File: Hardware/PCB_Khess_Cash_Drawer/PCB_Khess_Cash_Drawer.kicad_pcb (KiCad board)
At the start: 2 copper layers, 92 x 84 mm, 17 parts, among them J1 Screw_Terminal_01x02, J2 Conn_01x02, J3 RJ11_Connector, J4 USB3_A, Q1 BUK9637-100E,118, U1 R-78B5.0-2.0

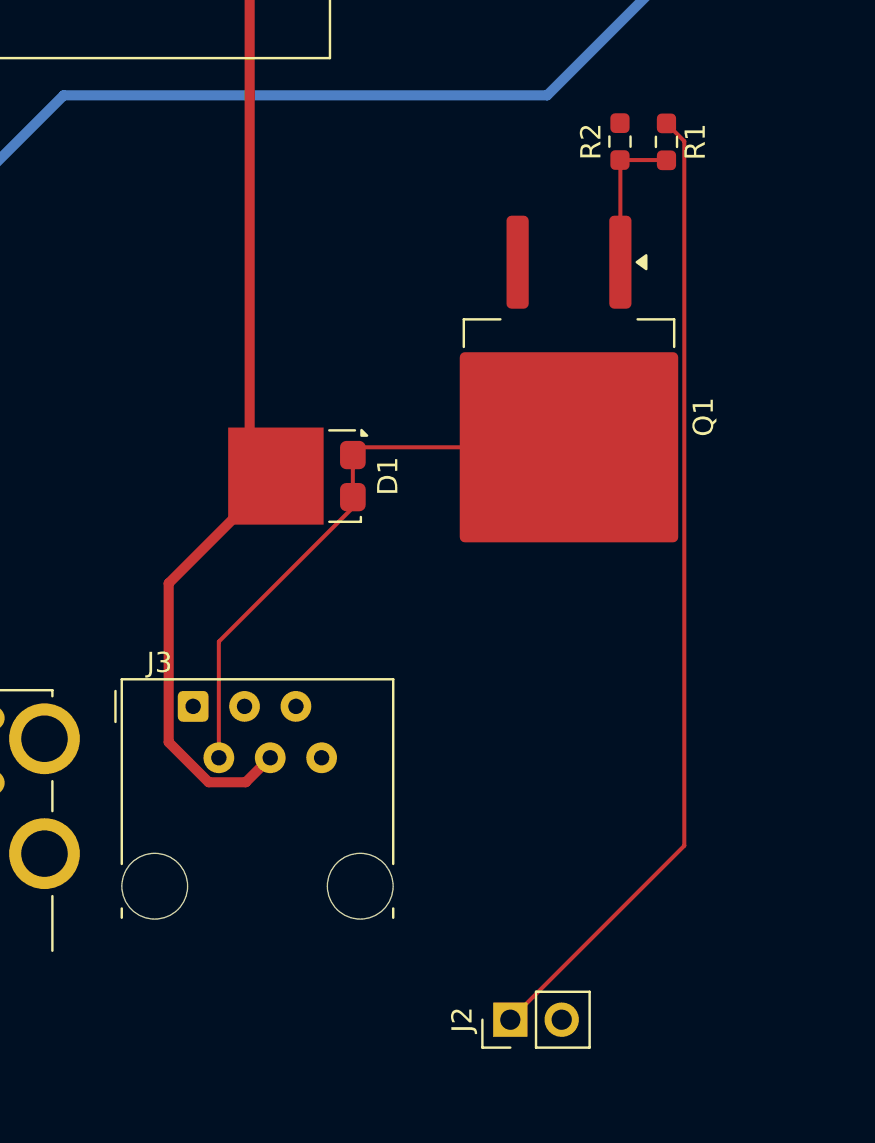
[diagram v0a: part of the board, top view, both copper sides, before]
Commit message: fix: fix pcb cash drawer
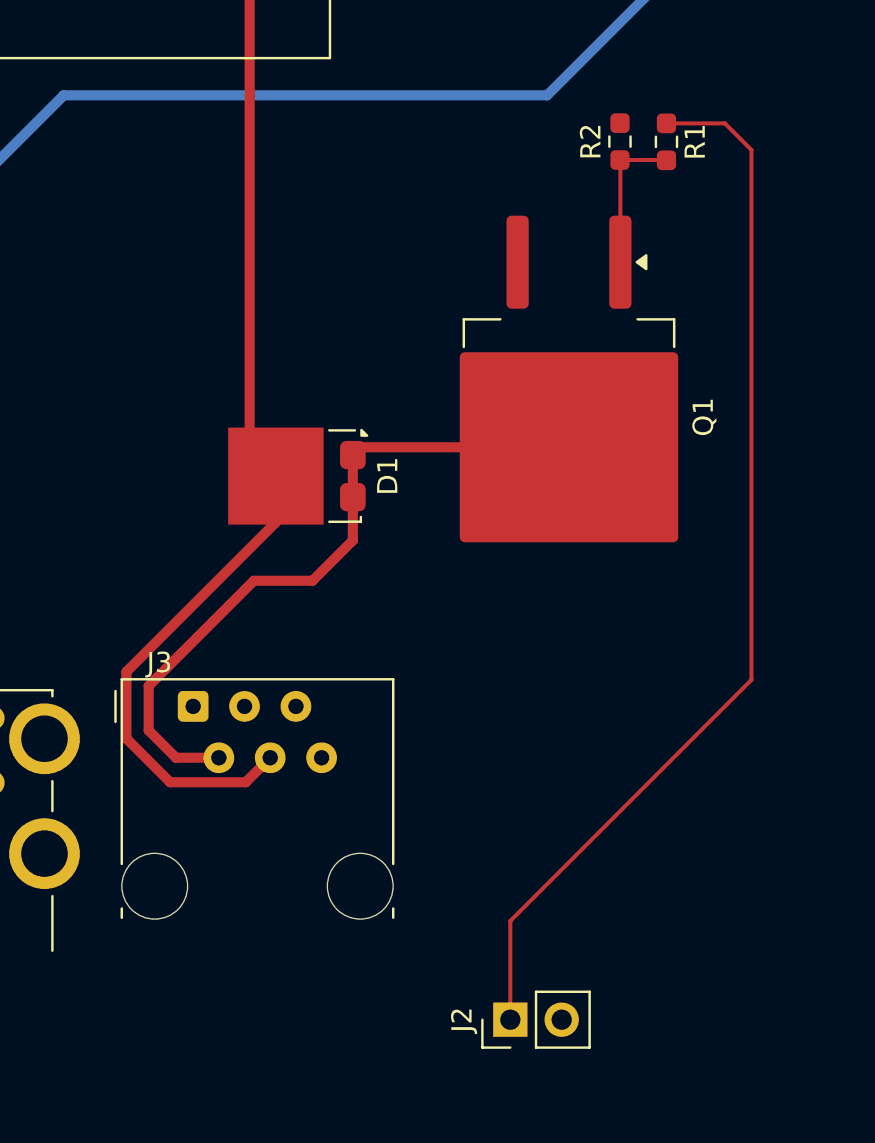
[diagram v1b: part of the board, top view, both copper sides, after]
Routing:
- net CASH_DRAWER_DRIVE: track 28.6 -> 34.9 mm
- net GPIO_CONTROL: track 48.2 -> 52.7 mm
- net CASH_DRAWER_VCC: track 63.1 -> 65.9 mm
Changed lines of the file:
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@@
 		(property ki_fp_filters "MountingHole*Pad*")
 		(sheetname "/")
-		(sheetfile "PCB_Khess.kicad_sch")
+		(sheetfile "PCB_Khess_Cash_Drawer.kicad_sch")
 		(attr exclude_from_pos_files)
 		(fp_circle
@@
 		(property ki_fp_filters "R_*")
 		(sheetname "/")
-		(sheetfile "PCB_Khess.kicad_sch")
+		(sheetfile "PCB_Khess_Cash_Drawer.kicad_sch")
 		(attr smd)
 		(fp_line
@@
 		(property ki_fp_filters "MountingHole*Pad*")
 		(sheetname "/")
-		(sheetfile "PCB_Khess.kicad_sch")
+		(sheetfile "PCB_Khess_Cash_Drawer.kicad_sch")
 		(attr exclude_from_pos_files)
 		(fp_circle
@@
 		(property ki_fp_filters "MountingHole*Pad*")
 		(sheetname "/")
-		(sheetfile "PCB_Khess.kicad_sch")
+		(sheetfile "PCB_Khess_Cash_Drawer.kicad_sch")
 		(attr exclude_from_pos_files)
 		(fp_circle
@@
 		(property ki_fp_filters "Converter*DCDC*RECOM*R*78B*2.0*")
 		(sheetname "/")
-		(sheetfile "PCB_Khess.kicad_sch")
+		(sheetfile "PCB_Khess_Cash_Drawer.kicad_sch")
 		(attr through_hole)
 		(fp_line
@@
 		)
 		(sheetname "/")
-		(sheetfile "PCB_Khess.kicad_sch")
+		(sheetfile "PCB_Khess_Cash_Drawer.kicad_sch")
 		(attr smd)
 		(fp_line
@@
 		(property ki_fp_filters "USB3*")
 		(sheetname "/")
-		(sheetfile "PCB_Khess.kicad_sch")
+		(sheetfile "PCB_Khess_Cash_Drawer.kicad_sch")
 		(attr through_hole)
 		(fp_line
@@
 		(property ki_fp_filters "Connector*:*_1x??_*")
 		(sheetname "/")
-		(sheetfile "PCB_Khess.kicad_sch")
+		(sheetfile "PCB_Khess_Cash_Drawer.kicad_sch")
 		(attr through_hole)
 		(fp_line
@@
 		(property ki_fp_filters "TO-???* *_Diode_* *SingleDiode* D_*")
 		(sheetname "/")
-		(sheetfile "PCB_Khess.kicad_sch")
+		(sheetfile "PCB_Khess_Cash_Drawer.kicad_sch")
 		(attr smd)
 		(fp_line
@@
 		(property ki_fp_filters "C_*")
 		(sheetname "/")
-		(sheetfile "PCB_Khess.kicad_sch")
+		(sheetfile "PCB_Khess_Cash_Drawer.kicad_sch")
 		(attr smd)
 		(fp_line
@@
 		(property ki_fp_filters "TerminalBlock*:*")
 		(sheetname "/")
-		(sheetfile "PCB_Khess.kicad_sch")
+		(sheetfile "PCB_Khess_Cash_Drawer.kicad_sch")
 		(attr through_hole)
 		(fp_line
@@
 		(property ki_fp_filters "Connector*:*_1x??-1MP*")
 		(sheetname "/")
-		(sheetfile "PCB_Khess.kicad_sch")
+		(sheetfile "PCB_Khess_Cash_Drawer.kicad_sch")
 		(attr through_hole)
 		(fp_line
@@
 		(property ki_fp_filters "Choke_* *Coil* Inductor_* L_*")
 		(sheetname "/")
-		(sheetfile "PCB_Khess.kicad_sch")
+		(sheetfile "PCB_Khess_Cash_Drawer.kicad_sch")
 		(attr smd)
 		(fp_line
@@
 		(property ki_fp_filters "R_*")
 		(sheetname "/")
-		(sheetfile "PCB_Khess.kicad_sch")
+		(sheetfile "PCB_Khess_Cash_Drawer.kicad_sch")
 		(attr smd)
 		(fp_line
@@
 		(property ki_fp_filters "MountingHole*Pad*")
 		(sheetname "/")
-		(sheetfile "PCB_Khess.kicad_sch")
+		(sheetfile "PCB_Khess_Cash_Drawer.kicad_sch")
 		(attr exclude_from_pos_files)
 		(fp_circle
@@
 		(property ki_fp_filters "C_*")
 		(sheetname "/")
-		(sheetfile "PCB_Khess.kicad_sch")
+		(sheetfile "PCB_Khess_Cash_Drawer.kicad_sch")
 		(attr smd)
 		(fp_line
@@
 		(property ki_fp_filters "Converter*ACDC*Hi?Link*HLK?PM*")
 		(sheetname "/")
-		(sheetfile "PCB_Khess.kicad_sch")
+		(sheetfile "PCB_Khess_Cash_Drawer.kicad_sch")
 		(attr through_hole)
 		(fp_line
@@
 	)
 	(segment
-		(start 121.6925 55.9075)
-		(end 125.1075 52.4925)
+		(start 115.6 92.9)
+		(end 122.99 85.51)
 		(width 0.5)
 		(layer "F.Cu")
@@
 	)
 	(segment
-		(start 117.689 88.526)
-		(end 122.99 83.225)
+		(start 121.6925 55.9075)
+		(end 125.1075 52.4925)
 		(width 0.5)
 		(layer "F.Cu")
@@
 	(segment
 		(start 121.499 98.361)
-		(end 119.668387 98.361)
+		(end 117.761 98.361)
 		(width 0.5)
 		(layer "F.Cu")
@@
 	)
 	(segment
-		(start 119.668387 98.361)
-		(end 117.689 96.381613)
+		(start 122.99 85.51)
+		(end 122.99 83.225)
 		(width 0.5)
 		(layer "F.Cu")
@@
 	)
 	(segment
-		(start 117.689 96.381613)
-		(end 117.689 88.526)
+		(start 115.6 96.2)
+		(end 115.6 92.9)
+		(width 0.5)
+		(layer "F.Cu")
+		(net 1)
+	)
+	(segment
+		(start 117.761 98.361)
+		(end 115.6 96.2)
 		(width 0.5)
 		(layer "F.Cu")
@@
 	)
 	(segment
-		(start 137.48 81.8)
-		(end 127.18 81.8)
-		(width 0.2)
+		(start 126.795 82.185)
+		(end 126.795 84.265)
+		(width 0.5)
 		(layer "F.Cu")
 		(net 4)
 	)
 	(segment
-		(start 126.795 84.265)
-		(end 126.795 82.185)
-		(width 0.2)
+		(start 116.7 93.6)
+		(end 121.9 88.4)
+		(width 0.5)
 		(layer "F.Cu")
 		(net 4)
@@
 		(start 127.18 81.8)
 		(end 126.795 82.185)
-		(width 0.2)
+		(width 0.5)
 		(layer "F.Cu")
 		(net 4)
@@
 	(segment
 		(start 120.17 97.15)
-		(end 120.17 91.407)
-		(width 0.2)
+		(end 118.05 97.15)
+		(width 0.5)
+		(layer "F.Cu")
+		(net 4)
+	)
+	(segment
+		(start 137.48 81.8)
+		(end 127.18 81.8)
+		(width 0.5)
 		(layer "F.Cu")
 		(net 4)
@@
 	)
 	(segment
-		(start 120.17 91.407)
-		(end 126.795 84.782)
-		(width 0.2)
+		(start 116.7 95.8)
+		(end 116.7 93.6)
+		(width 0.5)
+		(layer "F.Cu")
+		(net 4)
+	)
+	(segment
+		(start 126.795 86.405)
+		(end 126.795 84.265)
+		(width 0.5)
+		(layer "F.Cu")
+		(net 4)
+	)
+	(segment
+		(start 118.05 97.15)
+		(end 116.7 95.8)
+		(width 0.5)
+		(layer "F.Cu")
+		(net 4)
+	)
+	(segment
+		(start 124.8 88.4)
+		(end 126.795 86.405)
+		(width 0.5)
+		(layer "F.Cu")
+		(net 4)
+	)
+	(segment
+		(start 121.9 88.4)
+		(end 124.8 88.4)
+		(width 0.5)
 		(layer "F.Cu")
 		(net 4)
@@
 	)
 	(segment
-		(start 142.3 65.7875)
-		(end 143.181 66.6685)
+		(start 146.5 93.3)
+		(end 146.5 67.1)
+		(width 0.2)
+		(layer "F.Cu")
+		(net 7)
+	)
+	(segment
+		(start 146.5 67.1)
+		(end 145.1875 65.7875)
+		(width 0.2)
+		(layer "F.Cu")
+		(net 7)
+	)
+	(segment
+		(start 134.58 110.1)
+		(end 134.58 105.22)
 		(width 0.2)
 		(layer "F.Cu")
@@
 	)
 	(segment
-		(start 143.181 101.499)
-		(end 134.58 110.1)
+		(start 134.58 105.22)
+		(end 146.5 93.3)
 		(width 0.2)
 		(layer "F.Cu")
@@
 	)
 	(segment
-		(start 143.181 66.6685)
-		(end 143.181 101.499)
+		(start 145.1875 65.7875)
+		(end 142.3 65.7875)
 		(width 0.2)
 		(layer "F.Cu")

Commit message: fix: fix pcb
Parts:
- removed J4: USB3_A, Connector_USB:USB3_A_Molex_48406-0001_Horizontal_Stacked
- removed PS1: HLK-PM12, Converter_ACDC:Converter_ACDC_Hi-Link_HLK-PMxx
- added C4: 100u, Capacitor_SMD:CP_Elec_8x10, F.Cu at (176.0, 55.0)
- added C5: 1u, Capacitor_SMD:C_0805_2012Metric, F.Cu at (183.7, 52.6)
- added D2: D_TVS, Diode_SMD:D_SMA_Handsoldering, F.Cu at (189.4, 54.1)
- added F1: Fuse, Fuse:Fuseholder_Cylinder-5x20mm_Schurter_0031_8201_Horizontal_Open, F.Cu at (88.8, 49.0)
- added PS2: PSK-15E-12, PSK-15E-12:CONV_PSK-15E-12, F.Cu at (146.2, 50.5)
- added R3: 6.8, Resistor_SMD:R_2512_6332Metric_Pad1.40x3.35mm_HandSolder, F.Cu at (118.0, 49.0)
- added RV1: 10D561K, MOV-10D561K:VAR_MOV-10D561K, F.Cu at (115.0, 57.9)
- J2: value Conn_01x02 -> Conn_01x03; footprint Connector_PinHeader_2.54mm:PinHeader_1x02_P2.54mm_Vertical -> Connector_PinHeader_2.54mm:PinHeader_1x03_P2.54mm_Horizontal
- moved C1 42.2 mm to (170.7, 71.8)
- moved C2 42.2 mm to (172.4, 71.8)
- moved L1 42.2 mm to (171.6, 69.0)
- moved U1 42.2 mm to (180.1, 68.9)
- moved H4 34.7 mm to (187.0, 91.0)
- moved H3 29.0 mm to (187.0, 40.0)
- moved J2 27.0 mm to (130.0, 83.5), turned to -90 degrees
- moved D1 20.0 mm to (143.6, 87.4)
- moved Q1 20.0 mm to (157.0, 84.5)
- moved R2 20.0 mm to (159.5, 70.9)
- moved R1 20.0 mm to (161.8, 70.9)
- moved J3 19.7 mm to (110.4, 76.8)
- moved H2 19.0 mm to (80.0, 91.0)
- moved J1 0.30 mm to (81.6, 49.0)
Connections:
- net CASH_DRAWER_VCC renamed +12V
- J2 pad 1: GPIO_CONTROL -> +5V
- J2 pad 2: GND -> GPIO_CONTROL
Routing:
- net +12V: track 65.9 -> 139.9 mm
- net AC_NEUTRAL: track 11.0 -> 47.8 mm
- net CASH_DRAWER_DRIVE: track 34.9 -> 62.7 mm
- net +5V: track 89.0 -> 65.9 mm
- net AC_LINE_FUSE: track 0.00 -> 10.7 mm
- net AC_LINE_FUSE_R: track 0.00 -> 5.90 mm
- net GPIO_CONTROL: track 52.7 -> 47.8 mm
- net AC_LINE: track 11.0 -> 7.12 mm
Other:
- board size 92 x 84 mm -> 121 x 65 mm

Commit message: fix: update
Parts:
- moved J2 8.48 mm to (130.0, 92.0)
- moved J3 2.13 mm to (110.4, 78.9)
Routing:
- net GPIO_CONTROL: track 47.8 -> 56.3 mm
- net +5V: track 65.9 -> 74.4 mm
- net +12V: track 139.9 -> 146.1 mm
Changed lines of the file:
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@@
 	(footprint "Connector_PinHeader_2.54mm:PinHeader_1x03_P2.54mm_Horizontal"
 		(layer "F.Cu")
-		(at 130.04 83.515 -90)
+		(at 130.04 92 -90)
 		(descr "Through hole angled pin header, 1x03, 2.54mm pitch, 6mm pin length, single row")
 		(tags "Through hole angled pin header THT 1x03 2.54mm single row")
@@
 	(footprint "Connector_RJ:RJ12_Amphenol_54601-x06_Horizontal"
 		(layer "F.Cu")
-		(at 110.350001 76.81)
+		(at 110.350001 78.945)
 		(descr "RJ12 6P6C horizontal socket, plastic body, tab down, https://cdn.amphenol-icc.com/media/wysiwyg/files/drawing/c-bmj-0082.pdf")
 		(tags "RJ12 connector")
@@
 	)
 	(segment
-		(start 144.149 92.651)
-		(end 146.315 90.485)
+		(start 111.620001 89.820001)
+		(end 117.3 95.5)
 		(width 0.5)
 		(layer "F.Cu")
@@
 	)
 	(segment
-		(start 146.7 86)
-		(end 146.315 86.385)
+		(start 146.315 90.485)
+		(end 146.315 88.465)
 		(width 0.5)
 		(layer "F.Cu")
@@
 	)
 	(segment
-		(start 157 86)
-		(end 146.7 86)
+		(start 146.7 86)
+		(end 146.315 86.385)
 		(width 0.5)
 		(layer "F.Cu")
@@
 	)
 	(segment
-		(start 146.315 90.485)
-		(end 146.315 88.465)
+		(start 117.3 95.5)
+		(end 141.3 95.5)
 		(width 0.5)
 		(layer "F.Cu")
@@
 	)
 	(segment
-		(start 146.315 88.982)
-		(end 146.315 88.465)
-		(width 0.2)
-		(layer "F.Cu")
-		(net 3)
-	)
-	(segment
-		(start 111.620001 85.520001)
-		(end 111.620001 79.35)
+		(start 157 86)
+		(end 146.7 86)
 		(width 0.5)
 		(layer "F.Cu")
@@
 	)
 	(segment
-		(start 114.451 92.651)
-		(end 144.149 92.651)
-		(width 0.5)
+		(start 146.315 88.982)
+		(end 146.315 88.465)
+		(width 0.2)
 		(layer "F.Cu")
 		(net 3)
 	)
 	(segment
-		(start 111.620001 89.820001)
-		(end 114.451 92.651)
+		(start 141.3 95.5)
+		(end 146.315 90.485)
 		(width 0.5)
 		(layer "F.Cu")
@@
 	)
 	(segment
-		(start 111.620001 85.520001)
+		(start 111.620001 81.485)
 		(end 111.620001 89.820001)
 		(width 0.5)
@@
 	)
 	(segment
-		(start 127.5 74.8)
-		(end 130.04 72.26)
-		(width 0.2)
-		(layer "F.Cu")
-		(net 6)
-	)
-	(segment
 		(start 161.82 68.62)
-		(end 161.82 69.9875)
+		(end 160.8 67.6)
 		(width 0.2)
 		(layer "F.Cu")
@@
 	)
 	(segment
-		(start 134.7 67.6)
-		(end 160.8 67.6)
+		(start 161.82 69.9875)
+		(end 161.82 68.62)
 		(width 0.2)
 		(layer "F.Cu")
@@
 	)
 	(segment
-		(start 160.8 67.6)
-		(end 161.82 68.62)
+		(start 127.5 74.8)
+		(end 127.5 92)
 		(width 0.2)
 		(layer "F.Cu")
@@
 	)
 	(segment
-		(start 130.04 72.26)
-		(end 134.7 67.6)
+		(start 134.7 67.6)
+		(end 127.5 74.8)
 		(width 0.2)
 		(layer "F.Cu")
@@
 	)
 	(segment
-		(start 127.5 83.515)
-		(end 127.5 74.8)
+		(start 160.8 67.6)
+		(end 134.7 67.6)
 		(width 0.2)
 		(layer "F.Cu")
@@
 	)
 	(segment
-		(start 185.13 70.87)
-		(end 182 74)
+		(start 133.4 74)
+		(end 130.04 77.36)
 		(width 0.5)
 		(layer "B.Cu")
@@
 	)
 	(segment
-		(start 185.13 68.925)
-		(end 185.13 70.87)
+		(start 185.13 70.87)
+		(end 182 74)
 		(width 0.5)
 		(layer "B.Cu")
@@
 	)
 	(segment
-		(start 133.4 74)
-		(end 130.04 77.36)
+		(start 182 74)
+		(end 133.4 74)
 		(width 0.5)
 		(layer "B.Cu")
@@
 	)
 	(segment
-		(start 182 74)
-		(end 133.4 74)
+		(start 130.04 77.36)
+		(end 130.04 92)
 		(width 0.5)
 		(layer "B.Cu")
@@
 	)
 	(segment
-		(start 130.04 77.36)
-		(end 130.04 83.515)
+		(start 185.13 68.925)
+		(end 185.13 70.87)
 		(width 0.5)
 		(layer "B.Cu")
@@
 	)
 	(segment
-		(start 142.109 87.826)
-		(end 115.926 87.826)
-		(width 0.5)
-		(layer "F.Cu")
-		(net 13)
-	)
-	(segment
-		(start 115.926 87.826)
-		(end 114.160001 86.060001)
+		(start 142.51 82.99)
+		(end 142.51 87.425)
 		(width 0.5)
 		(layer "F.Cu")
@@
 	)
 	(segment
-		(start 142.51 82.99)
-		(end 142.51 87.425)
+		(start 142.51 91.74)
+		(end 140.5 93.75)
 		(width 0.5)
 		(layer "F.Cu")
@@
 	)
 	(segment
-		(start 114.160001 86.060001)
-		(end 114.160001 79.35)
+		(start 142.51 87.425)
+		(end 142.51 91.74)
 		(width 0.5)
 		(layer "F.Cu")
@@
 	)
 	(segment
+		(start 121.25 93.75)
+		(end 114.160001 86.660001)
+		(width 0.5)
+		(layer "F.Cu")
+		(net 13)
+	)
+	(segment
+		(start 114.160001 86.660001)
+		(end 114.160001 81.485)
+		(width 0.5)
+		(layer "F.Cu")
+		(net 13)
+	)
+	(segment
 		(start 170.6975 70.97)
 		(end 170.6975 69.0325)
@@
 		(width 0.5)
 		(layer "F.Cu")
+		(net 13)
+	)
+	(segment
+		(start 140.5 93.75)
+		(end 121.25 93.75)
+		(width 0.5)
+		(layer "F.Cu")

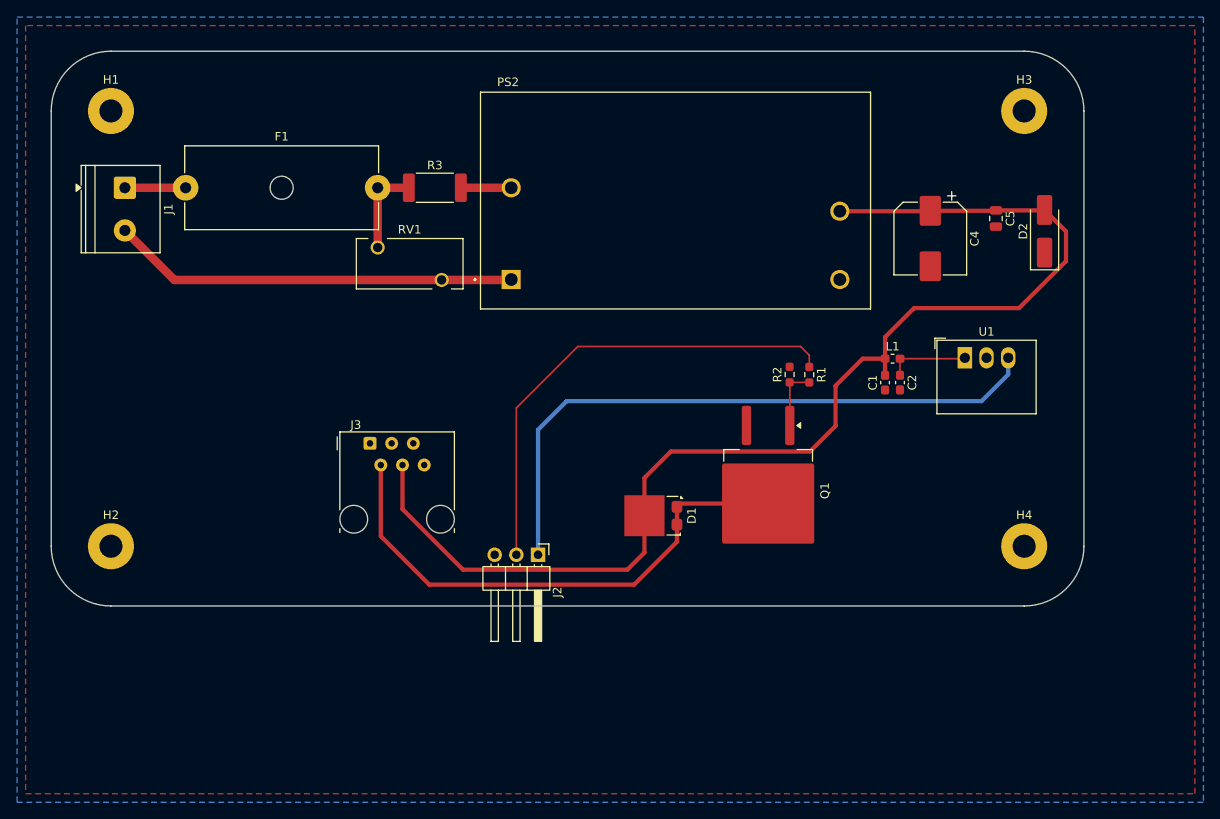
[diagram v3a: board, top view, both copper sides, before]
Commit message: fix: update two pcb and add gnd via
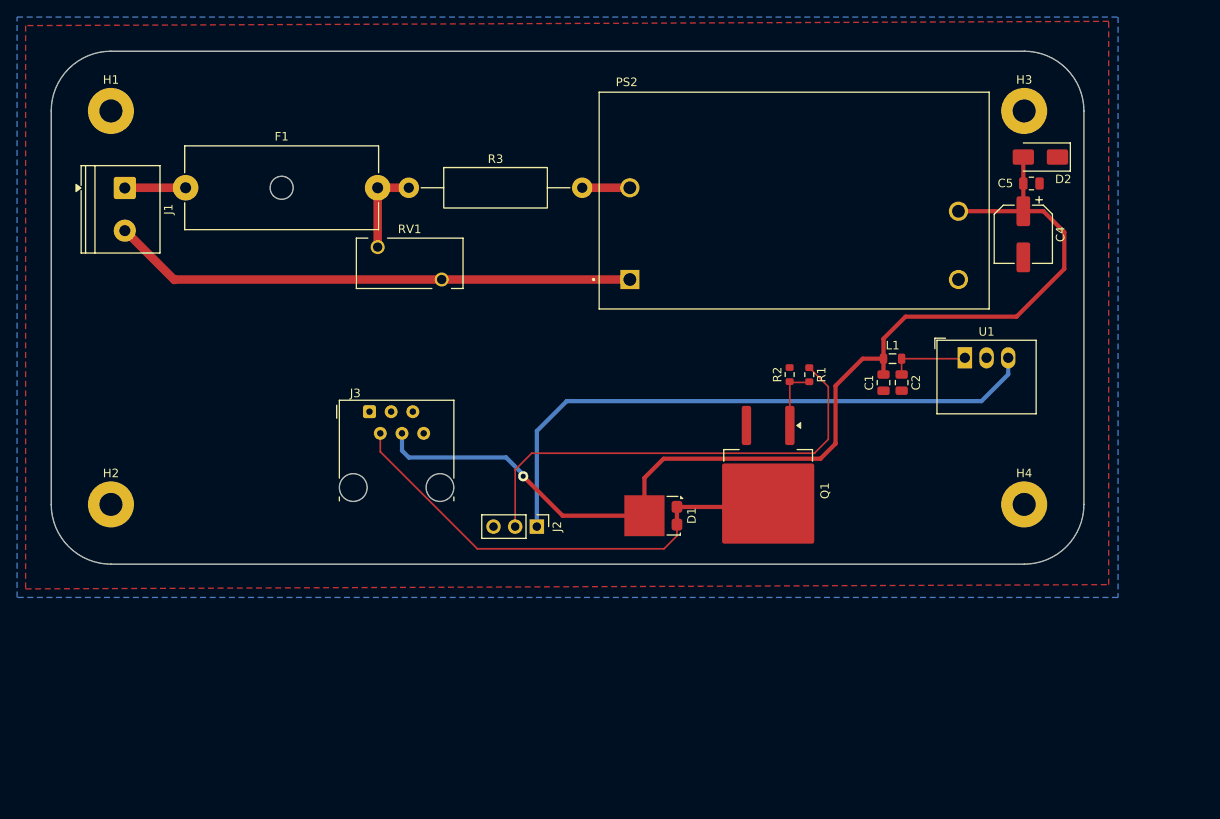
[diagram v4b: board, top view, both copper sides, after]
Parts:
- C1: footprint Capacitor_SMD:C_0603_1608Metric_Pad1.08x0.95mm_HandSolder -> Capacitor_SMD:C_0805_2012Metric
- C2: value 4.7u -> 4u7; footprint Capacitor_SMD:C_0603_1608Metric_Pad1.08x0.95mm_HandSolder -> Capacitor_SMD:C_0805_2012Metric
- C4: footprint Capacitor_SMD:CP_Elec_8x10 -> Capacitor_SMD:CP_Elec_6.3x7.7
- D2: value D_TVS -> 824 500 500; footprint Diode_SMD:D_SMA_Handsoldering -> Diode_SMD:D_SMA
- J2: footprint Connector_PinHeader_2.54mm:PinHeader_1x03_P2.54mm_Horizontal -> Connector_PinHeader_2.54mm:PinHeader_1x03_P2.54mm_Vertical
- L1: footprint Inductor_SMD:L_0603_1608Metric_Pad1.05x0.95mm_HandSolder -> Inductor_SMD:L_0805_2012Metric
- R1, R2: footprint Resistor_SMD:R_0603_1608Metric_Pad0.98x0.95mm_HandSolder -> Resistor_SMD:R_0603_1608Metric
- R3: footprint Resistor_SMD:R_2512_6332Metric_Pad1.40x3.35mm_HandSolder -> Resistor_THT:R_Axial_DIN0414_L11.9mm_D4.5mm_P20.32mm_Horizontal
- moved PS2 13.9 mm to (160.1, 50.5)
- moved C4 10.9 mm to (186.9, 54.5)
- moved D2 8.71 mm to (188.9, 45.4), turned to 180 degrees
- moved C5 5.84 mm to (187.8, 48.5), turned to 0 degrees
- moved H2 4.90 mm to (80.0, 86.1)
- moved H4 4.90 mm to (187.0, 86.1)
- moved J3 3.71 mm to (110.3, 75.2)
- moved J2 3.30 mm to (129.9, 88.7)
- moved R3 3.05 mm to (114.9, 49.0)
- moved C2 0.19 mm to (172.6, 71.8)
- moved C1 0.18 mm to (170.5, 71.8)
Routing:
- net +12V: track 146.1 -> 131.9 mm, vias 0 -> 1
- net AC_NEUTRAL: track 47.8 -> 61.6 mm
- net CASH_DRAWER_DRIVE: track 62.9 -> 56.5 mm
- net +5V: track 74.4 -> 71.1 mm
- net GPIO_CONTROL: track 56.3 -> 54.2 mm
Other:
- board size 121 x 65 mm -> 121 x 60.1 mm
